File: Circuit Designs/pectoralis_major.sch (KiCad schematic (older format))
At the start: 32 parts

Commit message: created golgi_tendon_organ page
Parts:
- removed J?: Conn_01x16, Connectors:524651671, symbol Connector_Generic:Conn_01x16
- removed J? (x2): Conn_01x10, Connectors:0533071071, symbol Connector_Generic:Conn_01x10
- added J?: 0524651671, symbol CoE_Connector:0524651671
- added J? (x2): 0533071071, symbol CoE_Connector:0533071071
- added J?: 0524651071, symbol CoE_Connector:0524651071
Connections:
- wire segments 160 -> 186
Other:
- note added: "BULK CAPACITORS | When adequate bulk capacitance is used, the motor voltage remains stable and a high current can be quickly supplied."
- note added: "connected to avian pallium"
- note added: "connected to the heart"
- note removed: "goes to Flight Controller"
- note removed: "goes to Power Management System"
- moved on the sheet: C?

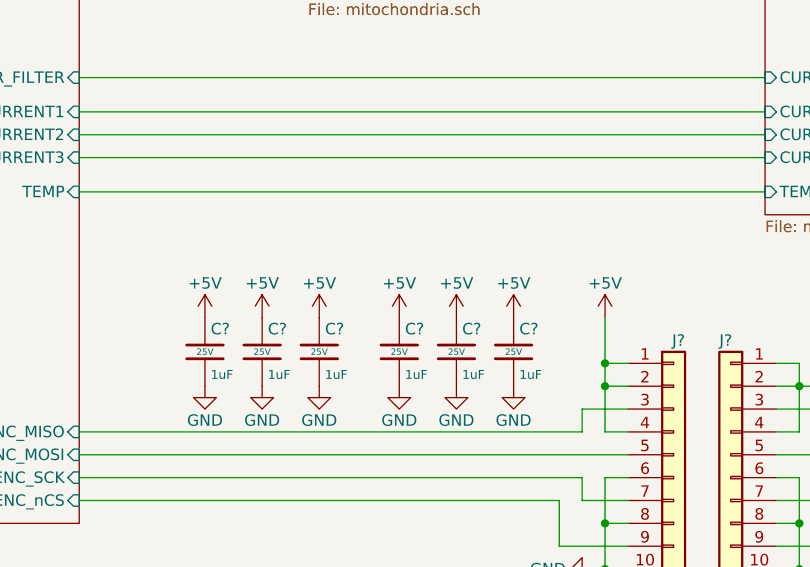
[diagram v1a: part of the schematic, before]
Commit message: added hal sensor
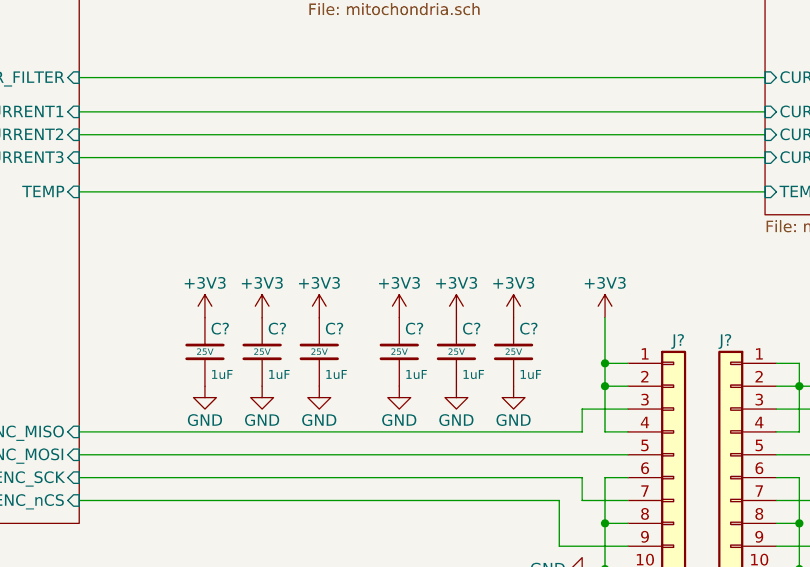
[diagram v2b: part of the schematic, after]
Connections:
- net +5V: no longer C?.1, C?.1, C?.1, C?.1, C?.1, C?.1, J?.1 (Pin_1), J?.2 (Pin_2), J?.4 (Pin_4)
- new net +3V3: C?.1, C?.1, C?.1, C?.1, C?.1, C?.1, J?.1 (Pin_1), J?.2 (Pin_2), J?.4 (Pin_4)
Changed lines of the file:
@@
 $EndComp
 Connection ~ 7800 6200
-$Comp
-L power:+5V #PWR?
-U 1 1 61CF506D
-P 7800 5100
-AR Path="/6171648E/61CF506D" Ref="#PWR?"  Part="1"
-AR Path="/617163B2/61CF506D" Ref="#PWR?"  Part="1"
-AR Path="/61CF506D" Ref="#PWR?"  Part="1"
-F 0 "#PWR?" H 7800 4950 50  0001 C CNN
-F 1 "+5V" H 7800 5250 50  0000 C CNN
-F 2 "" H 7800 5100 50  0001 C CNN
-F 3 "" H 7800 5100 50  0001 C CNN
-	1    7800 5100
-	1    0    0    -1
-$EndComp
 Wire Wire Line
 	7800 5100 7800 5300
@@
 	1    0    0    -1
 $EndComp
-$Comp
-L power:+5V #PWR?
-U 1 1 61D3C751
-P 6050 5100
-AR Path="/61D3C751" Ref="#PWR?"  Part="1"
-AR Path="/607CD6B1/61D3C751" Ref="#PWR?"  Part="1"
-AR Path="/6171648E/61D3C751" Ref="#PWR?"  Part="1"
-F 0 "#PWR?" H 6050 4950 50  0001 C CNN
-F 1 "+5V" H 6050 5250 50  0000 C CNN
-F 2 "" H 6050 5100 50  0001 C CNN
-F 3 "" H 6050 5100 50  0001 C CNN
-	1    6050 5100
-	1    0    0    -1
-$EndComp
 Wire Wire Line
 	1400 3700 2000 3700
@@
 $EndComp
 $Comp
-L power:+5V #PWR?
-U 1 1 6240D892
-P 6300 5100
-AR Path="/6240D892" Ref="#PWR?"  Part="1"
-AR Path="/607CD6B1/6240D892" Ref="#PWR?"  Part="1"
-AR Path="/6171648E/6240D892" Ref="#PWR?"  Part="1"
-F 0 "#PWR?" H 6300 4950 50  0001 C CNN
-F 1 "+5V" H 6300 5250 50  0000 C CNN
-F 2 "" H 6300 5100 50  0001 C CNN
-F 3 "" H 6300 5100 50  0001 C CNN
-	1    6300 5100
-	1    0    0    -1
-$EndComp
-$Comp
 L CoE_Capacitor:1uF C?
 U 1 1 6240D89B
@@
 $EndComp
 $Comp
-L power:+5V #PWR?
-U 1 1 62417C4C
-P 6550 5100
-AR Path="/62417C4C" Ref="#PWR?"  Part="1"
-AR Path="/607CD6B1/62417C4C" Ref="#PWR?"  Part="1"
-AR Path="/6171648E/62417C4C" Ref="#PWR?"  Part="1"
-F 0 "#PWR?" H 6550 4950 50  0001 C CNN
-F 1 "+5V" H 6550 5250 50  0000 C CNN
-F 2 "" H 6550 5100 50  0001 C CNN
-F 3 "" H 6550 5100 50  0001 C CNN
-	1    6550 5100
-	1    0    0    -1
-$EndComp
-$Comp
 L CoE_Capacitor:1uF C?
 U 1 1 62417C55
@@
 $EndComp
 $Comp
-L power:+5V #PWR?
-U 1 1 62421CCA
-P 6900 5100
-AR Path="/62421CCA" Ref="#PWR?"  Part="1"
-AR Path="/607CD6B1/62421CCA" Ref="#PWR?"  Part="1"
-AR Path="/6171648E/62421CCA" Ref="#PWR?"  Part="1"
-F 0 "#PWR?" H 6900 4950 50  0001 C CNN
-F 1 "+5V" H 6900 5250 50  0000 C CNN
-F 2 "" H 6900 5100 50  0001 C CNN
-F 3 "" H 6900 5100 50  0001 C CNN
-	1    6900 5100
-	1    0    0    -1
-$EndComp
-$Comp
 L CoE_Capacitor:1uF C?
 U 1 1 62421CD3
@@
 $EndComp
 $Comp
-L power:+5V #PWR?
-U 1 1 6242BF34
-P 7150 5100
-AR Path="/6242BF34" Ref="#PWR?"  Part="1"
-AR Path="/607CD6B1/6242BF34" Ref="#PWR?"  Part="1"
-AR Path="/6171648E/6242BF34" Ref="#PWR?"  Part="1"
-F 0 "#PWR?" H 7150 4950 50  0001 C CNN
-F 1 "+5V" H 7150 5250 50  0000 C CNN
-F 2 "" H 7150 5100 50  0001 C CNN
-F 3 "" H 7150 5100 50  0001 C CNN
-	1    7150 5100
-	1    0    0    -1
-$EndComp
-$Comp
 L CoE_Capacitor:1uF C?
 U 1 1 6242BF3D
@@
 $EndComp
 $Comp
-L power:+5V #PWR?
-U 1 1 62436318
-P 7400 5100
-AR Path="/62436318" Ref="#PWR?"  Part="1"
-AR Path="/607CD6B1/62436318" Ref="#PWR?"  Part="1"
-AR Path="/6171648E/62436318" Ref="#PWR?"  Part="1"
-F 0 "#PWR?" H 7400 4950 50  0001 C CNN
-F 1 "+5V" H 7400 5250 50  0000 C CNN
-F 2 "" H 7400 5100 50  0001 C CNN
-F 3 "" H 7400 5100 50  0001 C CNN
-	1    7400 5100
-	1    0    0    -1
-$EndComp
-$Comp
 L CoE_Capacitor:1uF C?
 U 1 1 62436321
@@
 Data
 89 50 4E 47 0D 0A 1A 0A 00 00 00 0D 49 48 44 52 00 00 02 94 00 00 02 E9 08 02 00 00 00 82 11 21
-74 00 00 00 03 73 42 49 54 08 08 08 DB E1 4F E0 00 00 00 09 70 48 59 73 00 00 0B 12 00 00 0B 12
-01 D2 DD 7E FC 00 00 20 00 49 44 41 54 78 9C BC BD 79 B8 75 47 51 2F FC AB EA B5 F6 3E E7 9D 33
+74 00 00 00 03 73 42 49 54 08 08 08 DB E1 4F E0 00 00 00 09 70 48 59 73 00 00 0A F0 00 00 0A F0
+01 42 AC 34 98 00 00 20 00 49 44 41 54 78 9C BC BD 79 B8 75 47 51 2F FC AB EA B5 F6 3E E7 9D 33
 8F 90 89 84 24 10 41 42 18 45 10 C3 14 99 3E 45 EF 27 22 9F E0 23 E2 80 28 72 11 15 E5 62 14 15
 44 51 51 EF C5 CB A0 02 F2 08 01 14 01 91 C8 28 48 00 09 61 48 98 12 C0 0C 64 E4 CD 3B 9C 61 EF
@@
 	8950 6000 9700 6000
 Connection ~ 8650 6200
+$Comp
+L power:+3V3 #PWR?
+U 1 1 6214B190
+P 6050 5100
+AR Path="/620004B5/6214B190" Ref="#PWR?"  Part="1"
+AR Path="/6214B190" Ref="#PWR?"  Part="1"
+F 0 "#PWR?" H 6050 4950 50  0001 C CNN
+F 1 "+3V3" H 6050 5250 50  0000 C CNN
+F 2 "" H 6050 5100 50  0001 C CNN
+F 3 "" H 6050 5100 50  0001 C CNN
+	1    6050 5100
+	1    0    0    -1
+$EndComp
+$Comp
+L power:+3V3 #PWR?
+U 1 1 62157404
+P 6300 5100
+AR Path="/620004B5/62157404" Ref="#PWR?"  Part="1"
+AR Path="/62157404" Ref="#PWR?"  Part="1"
+F 0 "#PWR?" H 6300 4950 50  0001 C CNN
+F 1 "+3V3" H 6300 5250 50  0000 C CNN
+F 2 "" H 6300 5100 50  0001 C CNN
+F 3 "" H 6300 5100 50  0001 C CNN
+	1    6300 5100
+	1    0    0    -1
+$EndComp
+$Comp
+L power:+3V3 #PWR?
+U 1 1 62163777
+P 6550 5100
+AR Path="/620004B5/62163777" Ref="#PWR?"  Part="1"
+AR Path="/62163777" Ref="#PWR?"  Part="1"
+F 0 "#PWR?" H 6550 4950 50  0001 C CNN
+F 1 "+3V3" H 6550 5250 50  0000 C CNN
+F 2 "" H 6550 5100 50  0001 C CNN
+F 3 "" H 6550 5100 50  0001 C CNN
+	1    6550 5100
+	1    0    0    -1
+$EndComp
+$Comp
+L power:+3V3 #PWR?
+U 1 1 6216FCD5
+P 6900 5100
+AR Path="/620004B5/6216FCD5" Ref="#PWR?"  Part="1"
+AR Path="/6216FCD5" Ref="#PWR?"  Part="1"
+F 0 "#PWR?" H 6900 4950 50  0001 C CNN
+F 1 "+3V3" H 6900 5250 50  0000 C CNN
+F 2 "" H 6900 5100 50  0001 C CNN
+F 3 "" H 6900 5100 50  0001 C CNN
+	1    6900 5100
+	1    0    0    -1
+$EndComp
+$Comp
+L power:+3V3 #PWR?
+U 1 1 6217BF4E
+P 7150 5100
+AR Path="/620004B5/6217BF4E" Ref="#PWR?"  Part="1"
+AR Path="/6217BF4E" Ref="#PWR?"  Part="1"
+F 0 "#PWR?" H 7150 4950 50  0001 C CNN
+F 1 "+3V3" H 7150 5250 50  0000 C CNN
+F 2 "" H 7150 5100 50  0001 C CNN
+F 3 "" H 7150 5100 50  0001 C CNN
+	1    7150 5100
+	1    0    0    -1
+$EndComp
+$Comp
+L power:+3V3 #PWR?
+U 1 1 62188281
+P 7400 5100
+AR Path="/620004B5/62188281" Ref="#PWR?"  Part="1"
+AR Path="/62188281" Ref="#PWR?"  Part="1"
+F 0 "#PWR?" H 7400 4950 50  0001 C CNN
+F 1 "+3V3" H 7400 5250 50  0000 C CNN
+F 2 "" H 7400 5100 50  0001 C CNN
+F 3 "" H 7400 5100 50  0001 C CNN
+	1    7400 5100
+	1    0    0    -1
+$EndComp
+$Comp
+L power:+3V3 #PWR?
+U 1 1 62194666
+P 7800 5100
+AR Path="/620004B5/62194666" Ref="#PWR?"  Part="1"
+AR Path="/62194666" Ref="#PWR?"  Part="1"
+F 0 "#PWR?" H 7800 4950 50  0001 C CNN
+F 1 "+3V3" H 7800 5250 50  0000 C CNN
+F 2 "" H 7800 5100 50  0001 C CNN
+F 3 "" H 7800 5100 50  0001 C CNN
+	1    7800 5100
+	1    0    0    -1
+$EndComp
 $EndSCHEMATC

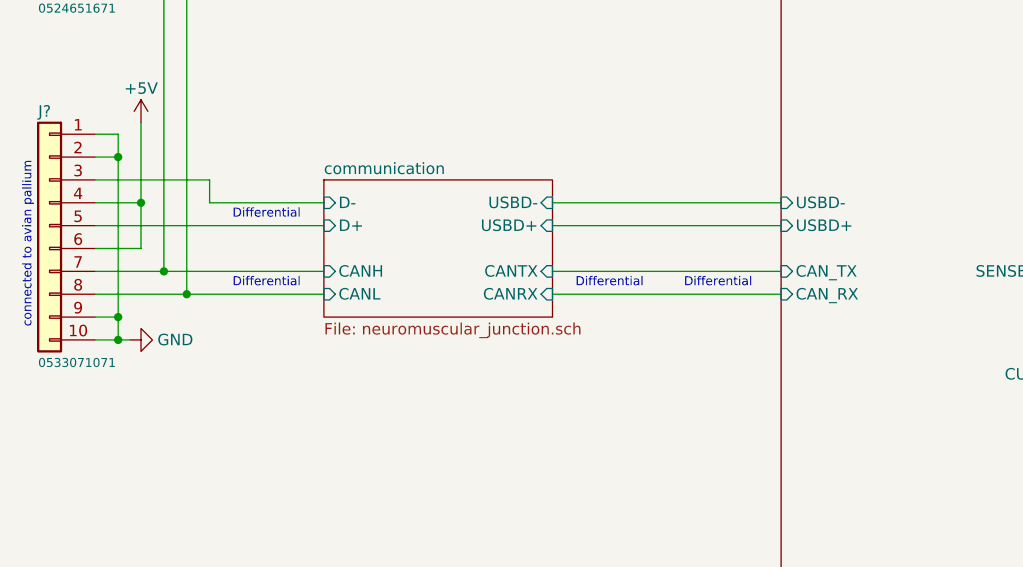
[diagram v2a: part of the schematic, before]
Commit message: added servo control input feature
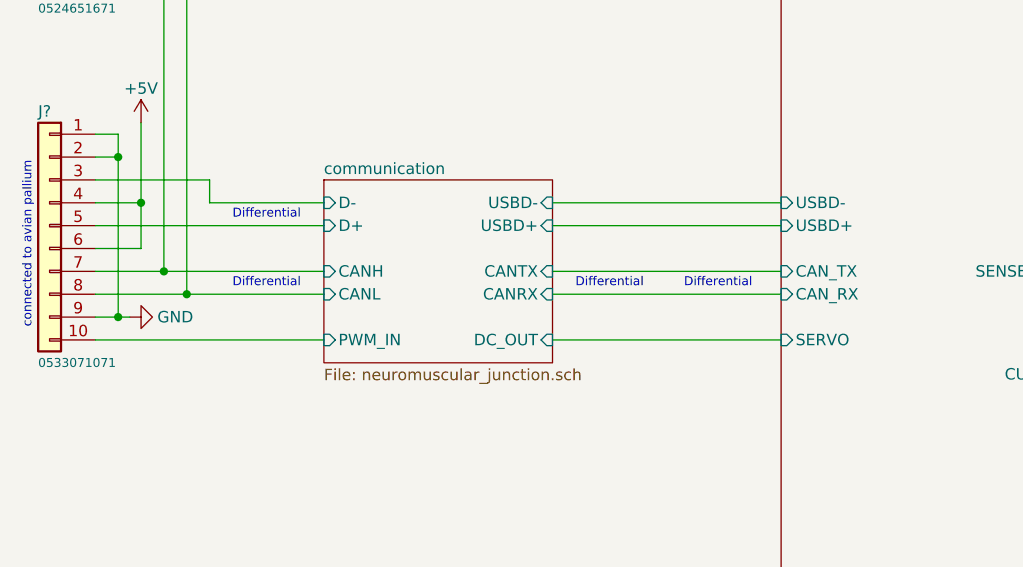
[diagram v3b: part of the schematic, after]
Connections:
- net GND: no longer J?.10 (Pin_10)
- new net communication/PWM_IN: J?.10 (Pin_10)
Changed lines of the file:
@@
 $EndDescr
 $Sheet
-S 2000 3200 1000 600
+S 2000 3200 1000 800
 U 620003D1
 F0 "communication" 50
@@
 F8 "CANTX" I R 3000 3600 50
 F9 "CANRX" I R 3000 3700 50
+F10 "PWM_IN" I L 2000 3900 50
+F11 "DC_OUT" I R 3000 3900 50
 $EndSheet
 $Sheet
@@
 F30 "CURRENT1" I R 5500 4200 50
 F31 "CURR_FILTER" I R 5500 4050 50
+F32 "SERVO" I L 4000 3900 50
 $EndSheet
 $Sheet
@@
 	1100 3800 1000 3800
 Connection ~ 1100 3100
-Wire Wire Line
-	1100 3800 1100 3900
-Wire Wire Line
-	1100 3900 1000 3900
 Connection ~ 1100 3800
-Connection ~ 1100 3900
 $Comp
 L power:GND #PWR?
 U 1 1 61DA921D
-P 1150 3900
-F 0 "#PWR?" H 1150 3650 50  0001 C CNN
-F 1 "GND" V 1150 3700 50  0000 C CNN
-F 2 "" H 1150 3900 50  0001 C CNN
-F 3 "" H 1150 3900 50  0001 C CNN
-	1    1150 3900
+P 1150 3800
+F 0 "#PWR?" H 1150 3550 50  0001 C CNN
+F 1 "GND" V 1150 3600 50  0000 C CNN
+F 2 "" H 1150 3800 50  0001 C CNN
+F 3 "" H 1150 3800 50  0001 C CNN
+	1    1150 3800
 	0    -1   -1   0
 $EndComp
@@
 $EndComp
 Wire Wire Line
-	1150 3900 1100 3900
+	1150 3800 1100 3800
 Wire Wire Line
 	1200 2950 1200 3300
@@
 	1    0    0    -1
 $EndComp
+Wire Wire Line
+	3000 3900 4000 3900
+Wire Wire Line
+	1000 3900 2000 3900
 $EndSCHEMATC
